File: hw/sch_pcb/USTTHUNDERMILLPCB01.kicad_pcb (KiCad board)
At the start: 4 copper layers, 80 x 80 mm, 88 parts, among them J1 SM06B-GHS-TB, J2 SM03B-GHS-TB, J4 HEADER_2x03, J5 SM08B-GHS-TB, J6 SM06B-GHS-TB, SW1 KMT031 NGJ LHS C&K, U1 ISL21080DIH312Z-TK 1V25, U10 SN74LVC1G14QDCKRQ1, U11 SN74LVC1G14QDCKRQ1, U12 SN74LVC1G14QDCKRQ1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

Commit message: Update layout
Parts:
- removed R4: 100R, Resistor_SMD:R_0603_1608Metric
- SW1: value KMT031 NGJ LHS C&K -> SW_Push
- moved C13 29.8 mm to (151.9, 86.1), turned to 45 degrees
- moved C12 19.4 mm to (154.9, 91.9), turned to -135 degrees
- moved C14 18.6 mm to (157.2, 89.7), turned to 45 degrees
- moved L1 17.6 mm to (158.2, 93.1), turned to -45 degrees
- moved JP4 5.52 mm to (159.6, 108.2), turned to 0 degrees
- moved C10 5.05 mm to (164.4, 97.4), turned to -90 degrees
- moved C9 2.90 mm to (162.5, 97.5), turned to -90 degrees
- moved J2 0.71 mm to (163.7, 87.5)
- moved C1 0.30 mm to (167.6, 95.7)
- moved R26 0.15 mm to (151.7, 99.7)
- moved C2 0.07 mm to (177.7, 92.5)
- turned C16 to 0 degrees
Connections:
- net ROTOR_GND renamed GND
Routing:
- net +3.3VA: track 7.58 -> 44.7 mm, vias 0 -> 6
- net +3V3: track 195.1 -> 174.5 mm, vias 6 -> 5
- net /CPU/BTN: track 24.2 -> 28.4 mm
- net Net-(U2--): track 5.51 -> 8.92 mm
- net COUNT_3: track 33.7 -> 35.5 mm
- net GND: track 4.43 -> 2.97 mm, vias 29 -> 72
- net /CPU/TX1: track 60.6 -> 61.4 mm
- net /CPU/GEO_STAT: track 51.1 -> 51.8 mm
- net GNDA: vias 8 -> 15
- net (no net): vias 126 -> 0
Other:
- rule pad_to_mask_clearance: 0.2 -> 0.1

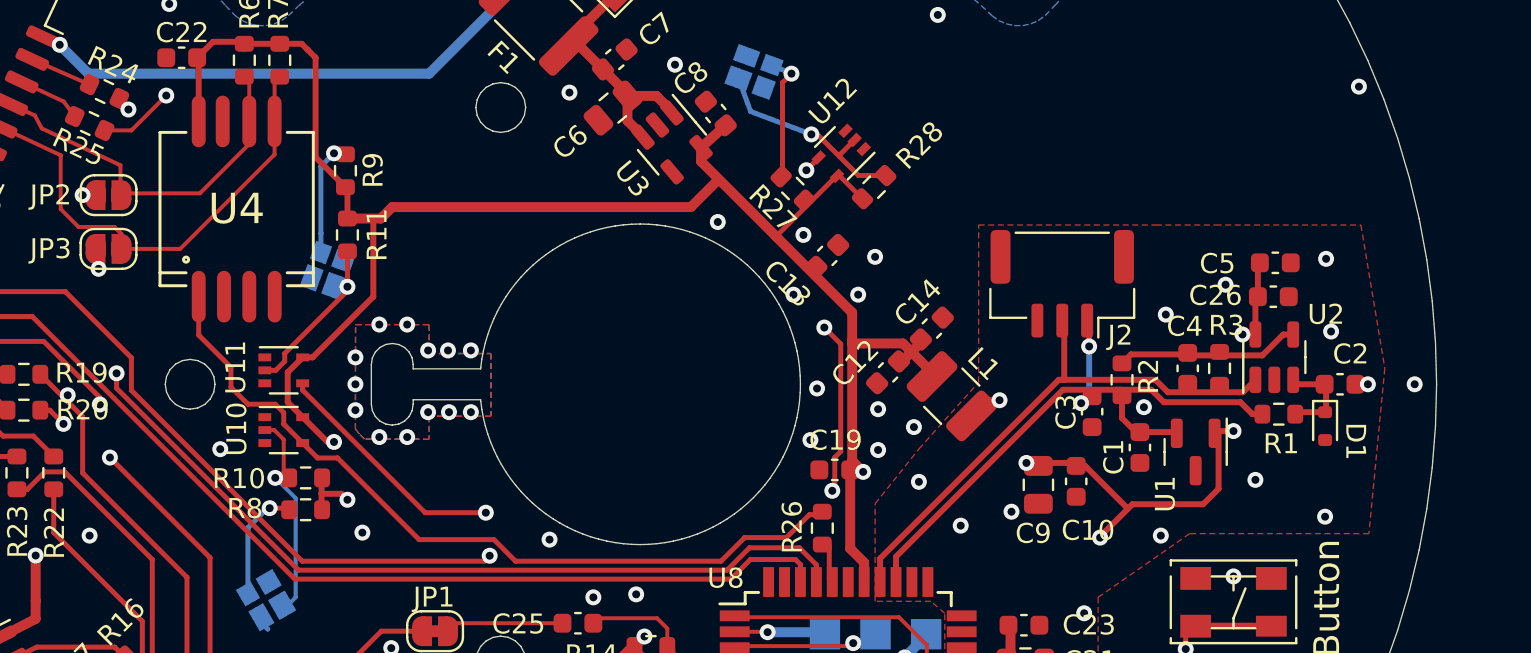
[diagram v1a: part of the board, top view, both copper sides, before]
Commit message: pridani testopintu pro pripojeni externi elektrody
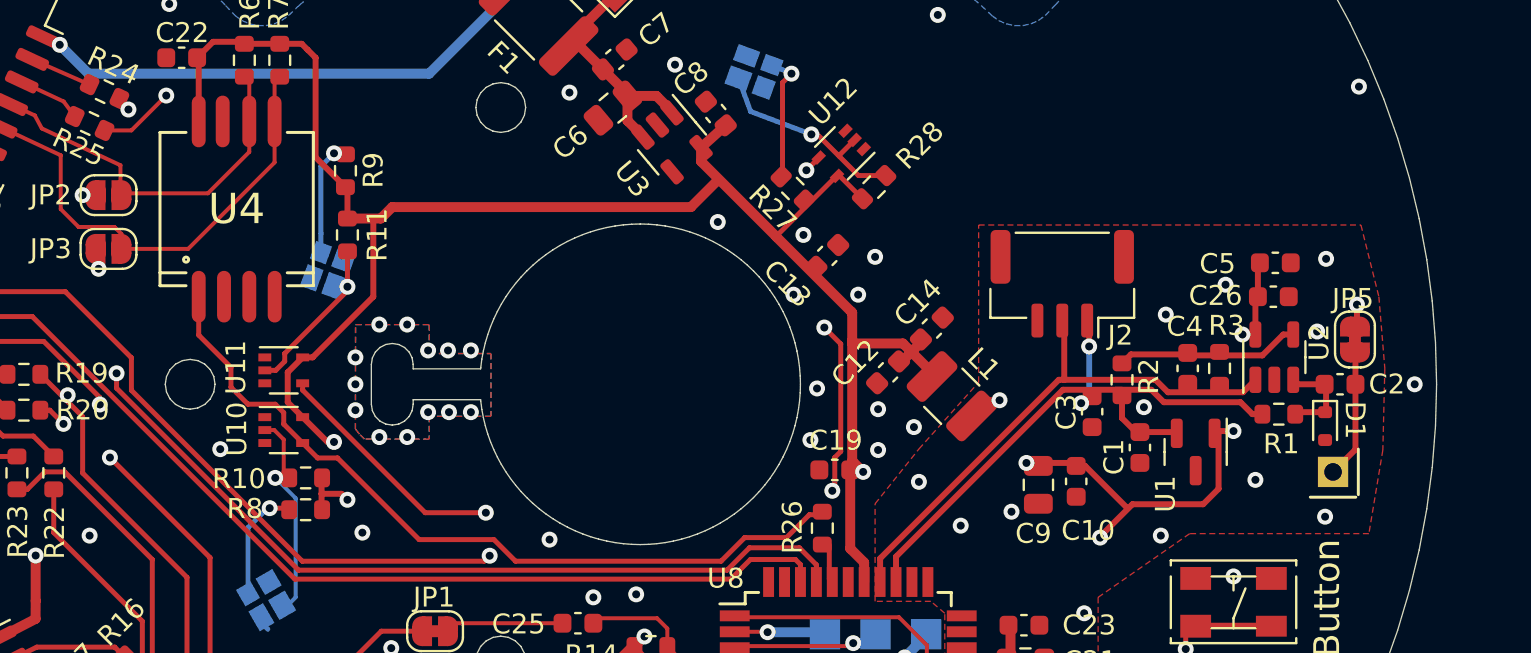
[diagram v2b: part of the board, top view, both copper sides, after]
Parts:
- added J3: HEADER_1x01, Mlab_Pin_Headers:Straight_1x01, F.Cu at (177.3, 96.9)
- added JP5: SolderJumper_2_Bridged, Jumper:SolderJumper-2_P1.3mm_Bridged_RoundedPad1.0x1.5mm, F.Cu at (178.4, 90.2)
- SW1: value SW_Push -> KMT031 NGJ LHS C&K
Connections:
- C2 pad 1: STATOR -> Net-(JP5-B)
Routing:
- net Net-(JP5-B): track 0.00 -> 6.44 mm
- net STATOR: track 0.39 -> 1.64 mm
